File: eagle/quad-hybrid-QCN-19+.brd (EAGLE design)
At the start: 20 x 20 mm, 6 parts, among them J1 142-0701-851, J2 142-0701-851, J3 142-0701-851, U1 QCN-19D+

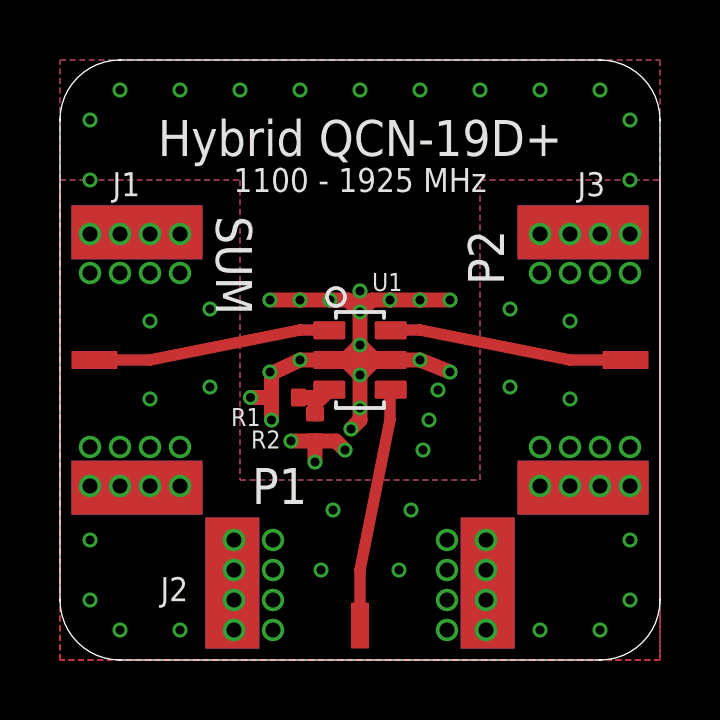
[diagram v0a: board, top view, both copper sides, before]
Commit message: Update QCN-19+ names
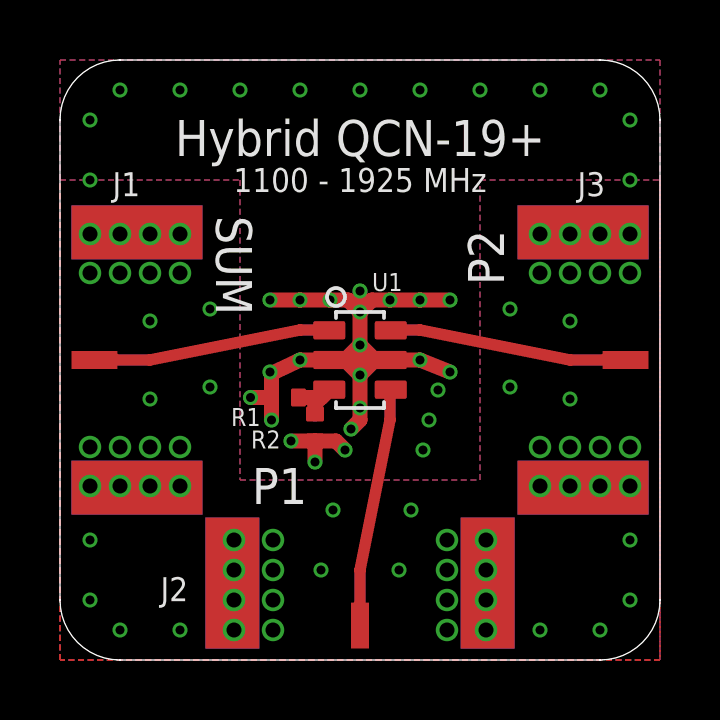
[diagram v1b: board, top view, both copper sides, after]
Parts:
- U1: value QCN-19D+ -> QCN-XXX+; device U-MiniCirc-QCN-19+-quad:QCN-19D+ -> U-MiniCirc-QCN-XXX+-quad:QCN-XXX+
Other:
- board text added: "Hybrid QCN-19+"
- board text added: "Quad. Hybrid QCN-19+ PSAS / OreSat 2019-11-05 v1 E.M. KJ7AOG"
- board text removed: "Hybrid QCN-19D+"
- board text removed: "Quad. Hybrid QCN-19D+ PSAS / OreSat 2019-11-05 v1 E.M. KJ7AOG"
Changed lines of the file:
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@@
 <drawing>
 <settings>
-<setting alwaysvectorfont="yes"/>
+<setting alwaysvectorfont="no"/>
 <setting verticaltext="up"/>
 </settings>
@@
 <wire x1="20" y1="10" x2="17" y2="10" width="2" layer="30"/>
 <wire x1="10" y1="0" x2="10" y2="3" width="2" layer="30"/>
-<text x="10" y="18.4" size="0.8" layer="22" font="vector" ratio="15" rot="MR0" align="top-center">Quad. Hybrid QCN-19D+
+<text x="10" y="18.4" size="0.8" layer="22" font="vector" ratio="15" rot="MR0" align="top-center">Quad. Hybrid QCN-19+
 PSAS / OreSat
 2019-11-05 v1
 E.M.  KJ7AOG</text>
-<text x="10" y="18" size="1.2" layer="21" font="vector" ratio="15" align="top-center">Hybrid QCN-19D+</text>
+<text x="10" y="18" size="1.2" layer="21" font="vector" ratio="15" align="top-center">Hybrid QCN-19+</text>
 <text x="10" y="16.4" size="0.8" layer="21" font="vector" ratio="15" align="top-center">1100 - 1925 MHz</text>
 <wire x1="0" y1="10" x2="3" y2="10" width="1.7" layer="29"/>
@@
 <attribute name="NAME" x="8.5" y="7.75" size="0.2" layer="33" ratio="15" rot="R90" align="center"/>
 </element>
-<element name="U1" library="U-MiniCirc-QCN-19+-quad" package="QCN-19D+" value="QCN-19D+" x="10" y="10" smashed="yes" rot="R270">
+<element name="U1" library="U-MiniCirc-QCN-XXX+-quad" package="QCN-XXX+" value="QCN-XXX+" x="10" y="10" smashed="yes" rot="R270">
 <attribute name="NAME" x="10.4" y="12.3" size="0.6" layer="21" font="vector" ratio="15"/>
 </element>

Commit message: Update QCN-19+, add optional isolation port
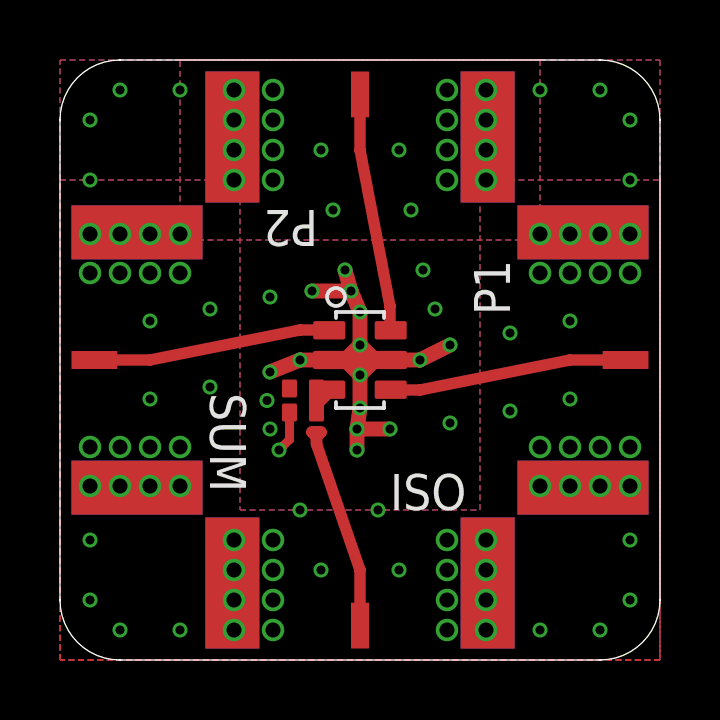
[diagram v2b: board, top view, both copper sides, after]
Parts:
- added J4: 142-0701-851, J-Cinch-142-0701-851-SMA-end-launch:142-0701-851
- moved J1 20.0 mm to (20.0, 10.0), turned to 270 degrees
- moved J2 20.0 mm to (10.0, 20.0), turned to 0 degrees
- moved J3 20.0 mm to (0.00, 10.0), turned to 90 degrees
- moved R2 1.36 mm to (8.10, 9.05), turned to 0 degrees
- moved R1 0.78 mm to (8.10, 8.25)
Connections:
- removed net PORT1: J2.RF1, U1.4
- removed net PORT2: J3.RF1, U1.6
- new net ISO: J4.RF1
- new net P1: J1.RF1, U1.4
- new net P2: J2.RF1, U1.6
- net GND: now also J4.GND1, J4.GND2, J4.GND3, J4.GND4
- net SUM: now also J3.RF1; no longer J1.RF1
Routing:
- net PORT1: track 7.97 -> 0.00 mm
- net P2: track 0.00 -> 7.97 mm
- net PORT2: track 7.93 -> 0.00 mm
- net P1: track 0.00 -> 7.93 mm
- net ISO: track 0.00 -> 7.49 mm
- net GND: track 26.1 -> 20.0 mm, vias 105 -> 117
- removed copper zone on layer 1, net PORT1
- removed copper zone on layer 1, net PORT2
- removed copper zone on layer 1, net SUM
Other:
- board text added: "ISO"
- board text added: "Quad. Hybrid QCN-19+ 1100 - 1925 MHz PSAS / OreSat 2019-11-06 v1 E.M. KJ7AOG"
- board text removed: "1100 - 1925 MHz"
- board text removed: "Hybrid QCN-19+"
- board text removed: "Quad. Hybrid QCN-19+ PSAS / OreSat 2019-11-05 v1 E.M. KJ7AOG"
